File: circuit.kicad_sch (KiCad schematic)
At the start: 27 parts, among them SW101 Pedal_1, SW102 Pedal_2, SW103 Pedal_3, SW104 Pedal_4, SW105 Pedal_5, SW106 Pedal_6, SW107 Pedal_7, SW108 Pedal_8, SW109 Program, SW110 Preset, U101 ESP32-S3-DevKitC

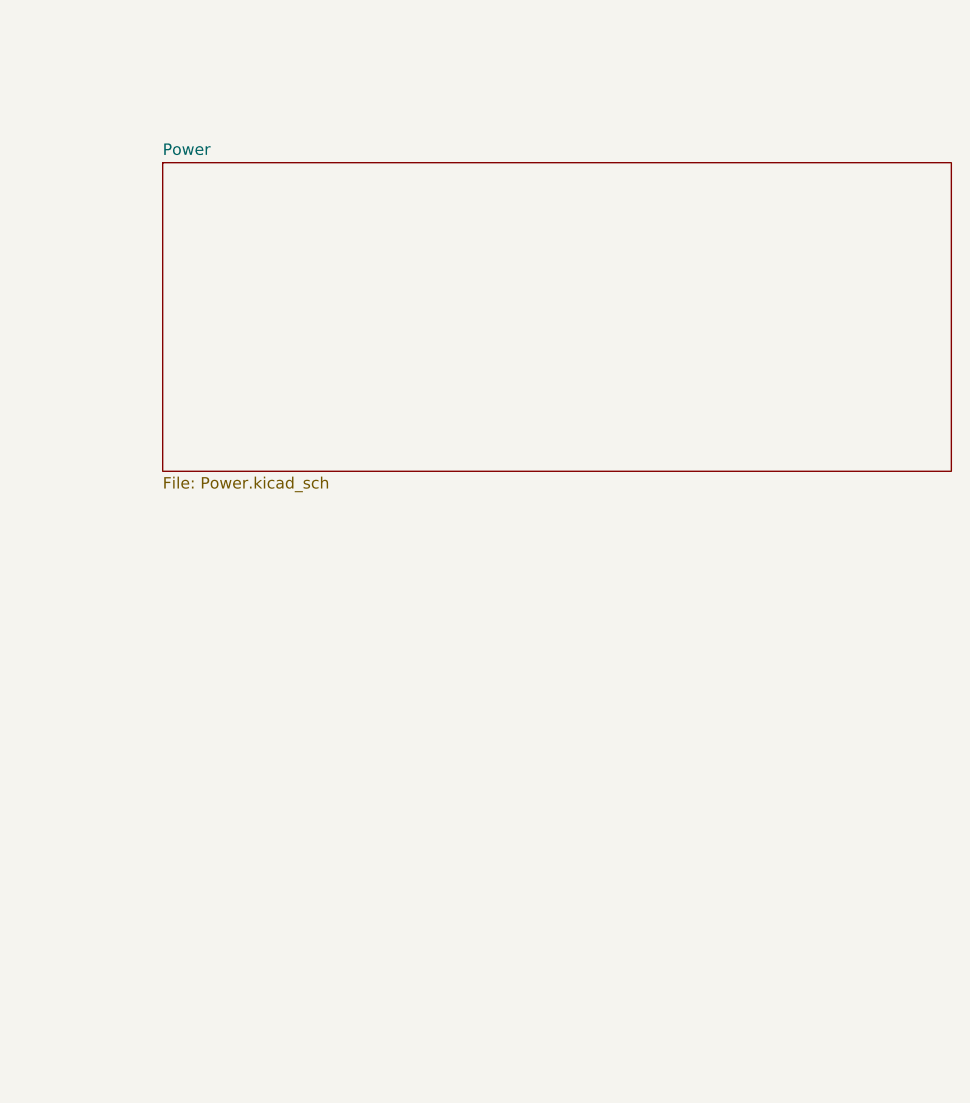
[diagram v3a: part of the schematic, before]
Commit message: Added Datasheets and specified polyfuse parameters.
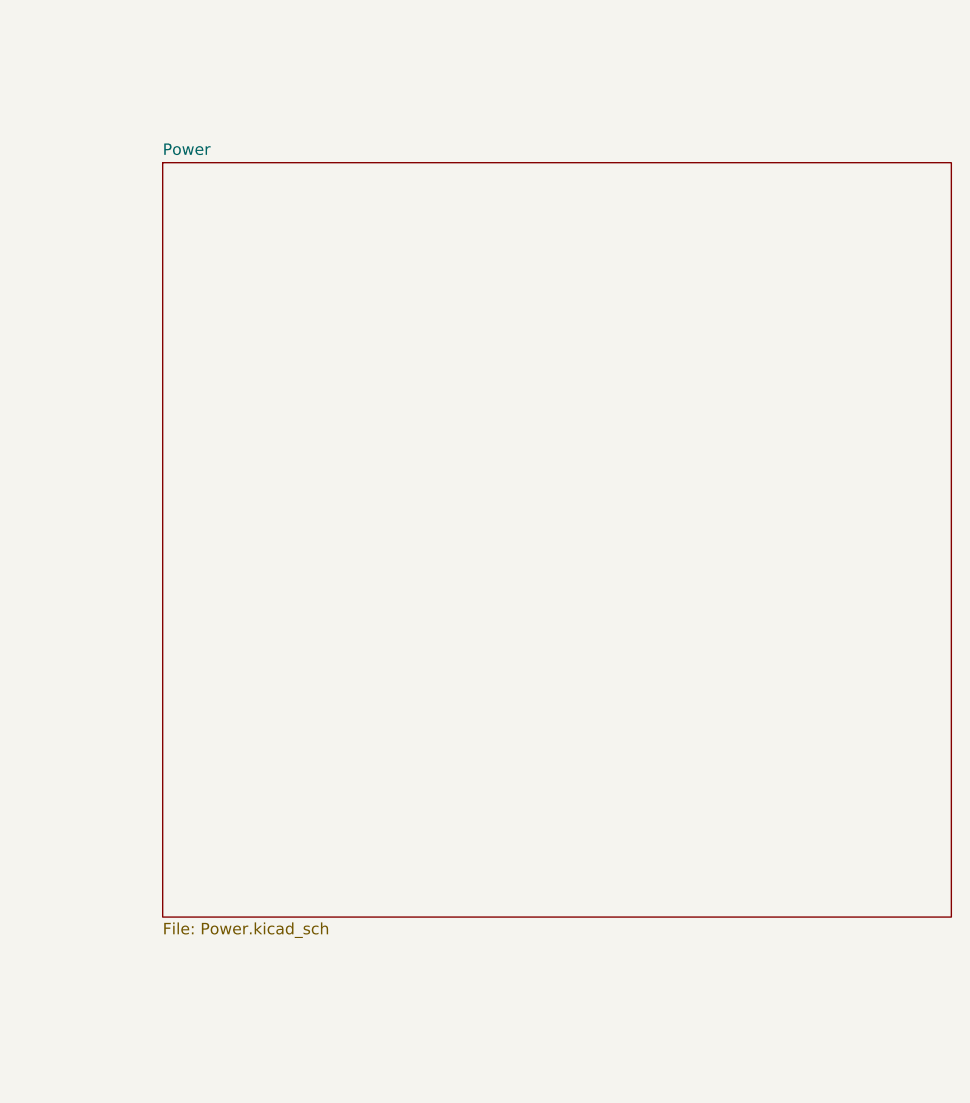
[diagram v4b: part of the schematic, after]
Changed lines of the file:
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@@
 	(sheet
 		(at 416.56 217.17)
-		(size 87.63 34.29)
+		(size 87.63 83.82)
 		(exclude_from_sim no)
 		(in_bom yes)
@@
 		)
 		(fill
-			(color 177 0 9 0.5000)
+			(color 0 0 0 0.0000)
 		)
 		(property "Sheetname" "Power"
@@
 		)
 		(property "Sheetfile" "Power.kicad_sch"
-			(at 416.56 252.0446 0)
+			(at 416.56 301.5746 0)
 			(effects
 				(font
@@
 		)
 		(fill
-			(color 25 155 0 0.5000)
+			(color 0 0 0 0.0000)
 		)
 		(property "Sheetname" "Buffers"
